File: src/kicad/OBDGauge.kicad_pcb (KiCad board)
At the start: 2 copper layers, 49.9 x 49.9 mm, 23 parts, among them J1 OBD, J2 Neopixel, J3 TM1637, J4 9V REG, Q1 3906, SW1 SW1, SW2 SW2, U1 LM2903

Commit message: Add files via upload
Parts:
- added R8: 10K, Resistor_THT:R_Axial_DIN0204_L3.6mm_D1.6mm_P7.62mm_Horizontal, B.Cu at (69.6, 57.0)
- moved R7 3.61 mm to (71.5, 58.1), turned to -120 degrees
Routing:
- net /12V: track 82.9 -> 93.2 mm
- net /K+: track 69.7 -> 74.2 mm
- net Net-(D2-A): track 4.03 -> 3.20 mm

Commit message: Add files via upload
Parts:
- added TEST3 LOG: GND, , F.Cu at (35.5, 68.0)
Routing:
- net /K-IN: track 14.9 -> 50.6 mm
- net GNDREF: track 176.6 -> 181.6 mm
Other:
- board text added: "OBD K-Line Gauge v1.2 (c)2024-2025 V. Lee Makermonkey Industries"
- board text removed: "OBD K-Line Gauge v1.1 (c)2024 V. Lee Makermonkey Industries"

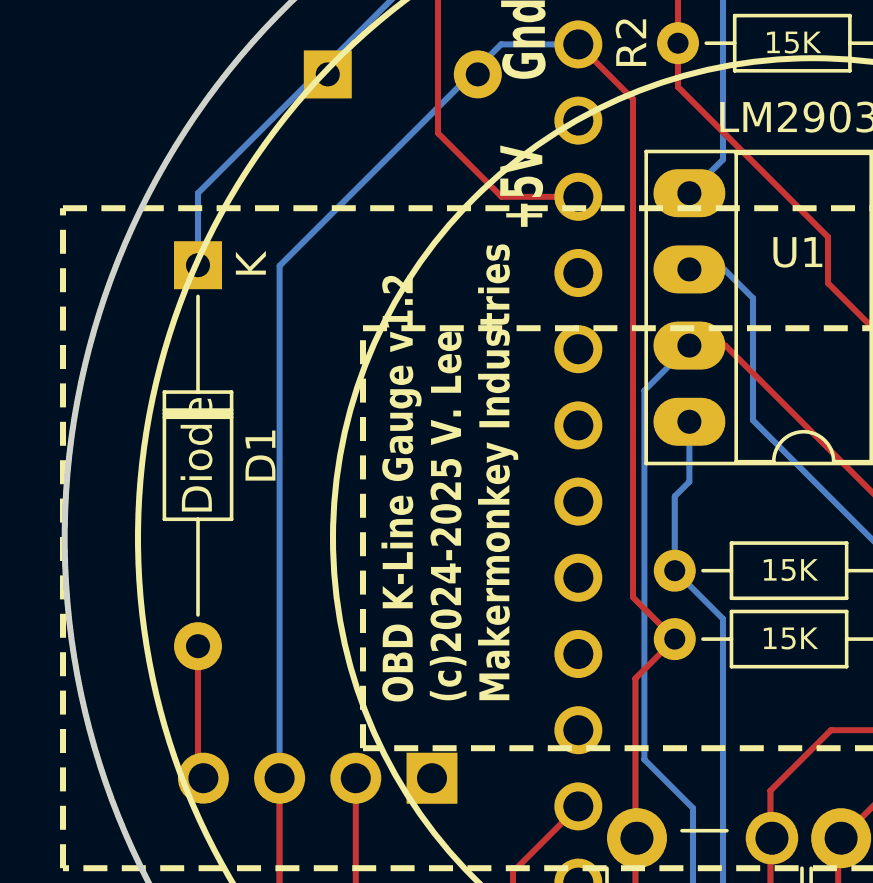
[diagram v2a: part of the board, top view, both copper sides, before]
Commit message: Updated to reflect Nano Every
Updated voltage divider value and note to reflect voltage regulator no longer needed for Nano Every.
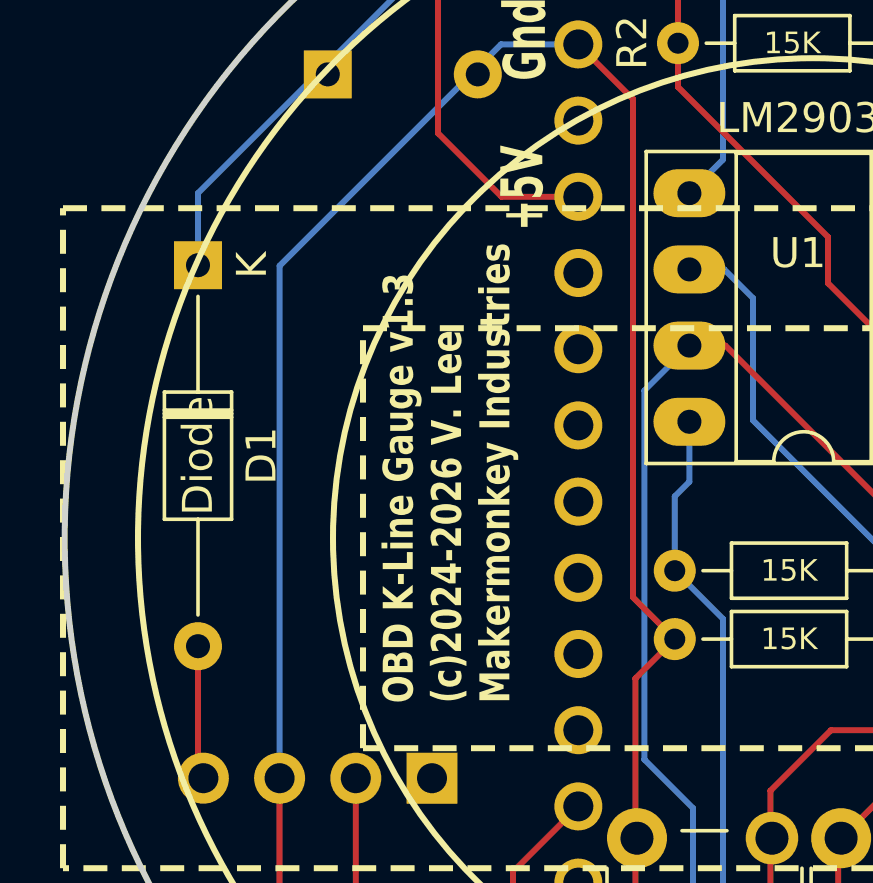
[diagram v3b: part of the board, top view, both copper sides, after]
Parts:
- A1: value NANO -> NANO EVERY
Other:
- board text added: "Bypass for Nano Every"
- board text added: "OBD K-Line Gauge v1.3 (c)2024-2026 V. Lee Makermonkey Industries"
- board text removed: "OBD K-Line Gauge v1.2 (c)2024-2025 V. Lee Makermonkey Industries"
